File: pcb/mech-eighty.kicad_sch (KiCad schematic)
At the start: 23 parts, among them SW1 Reset, SW2 SW_DPDT_x2, U1 STM32F103C8T6, U2 AMS1117-3.3, Y1 8MHz

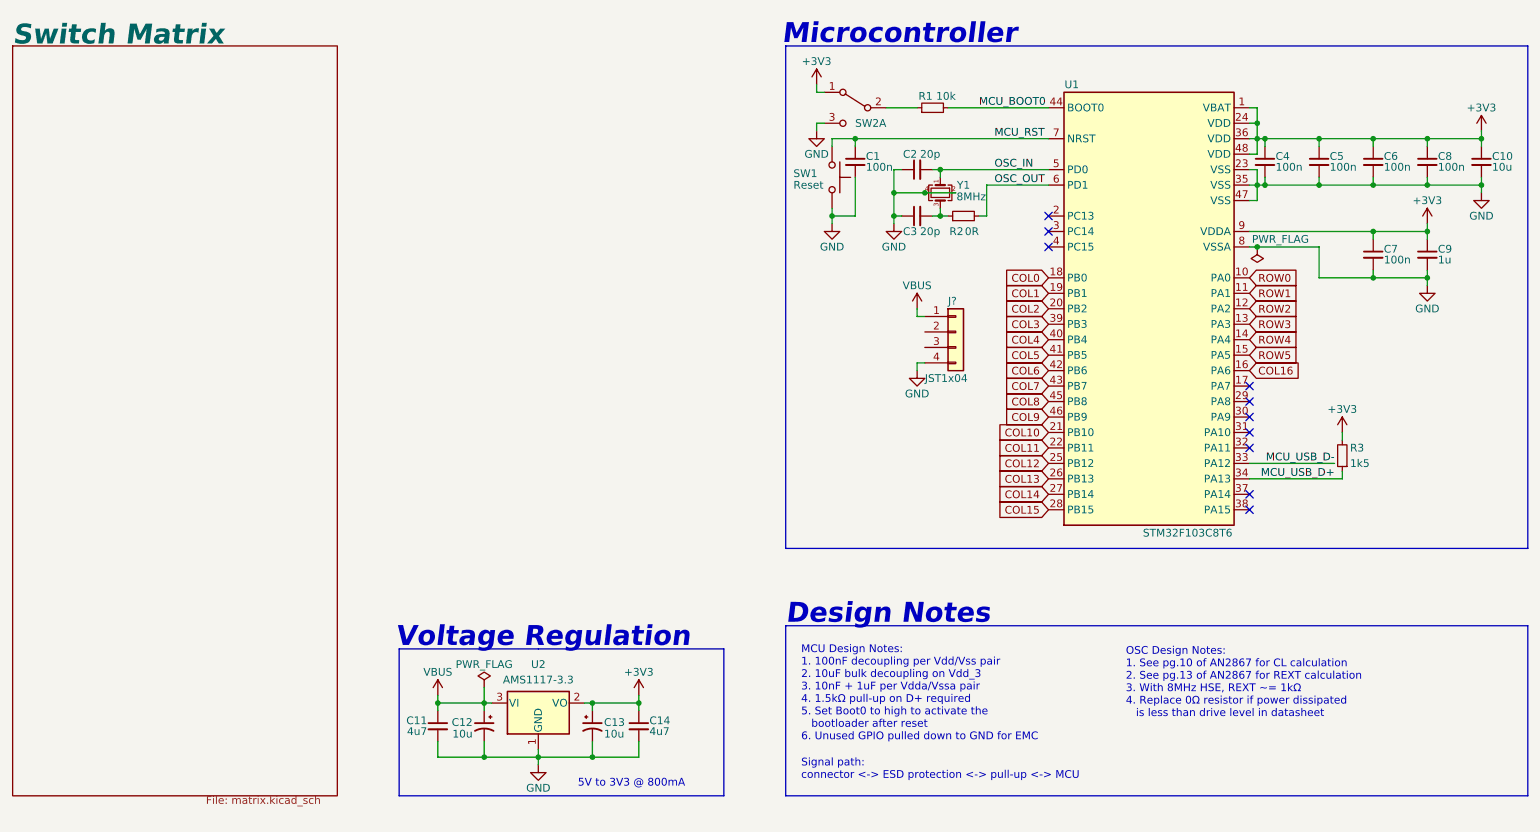
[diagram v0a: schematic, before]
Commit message: Schematic completed
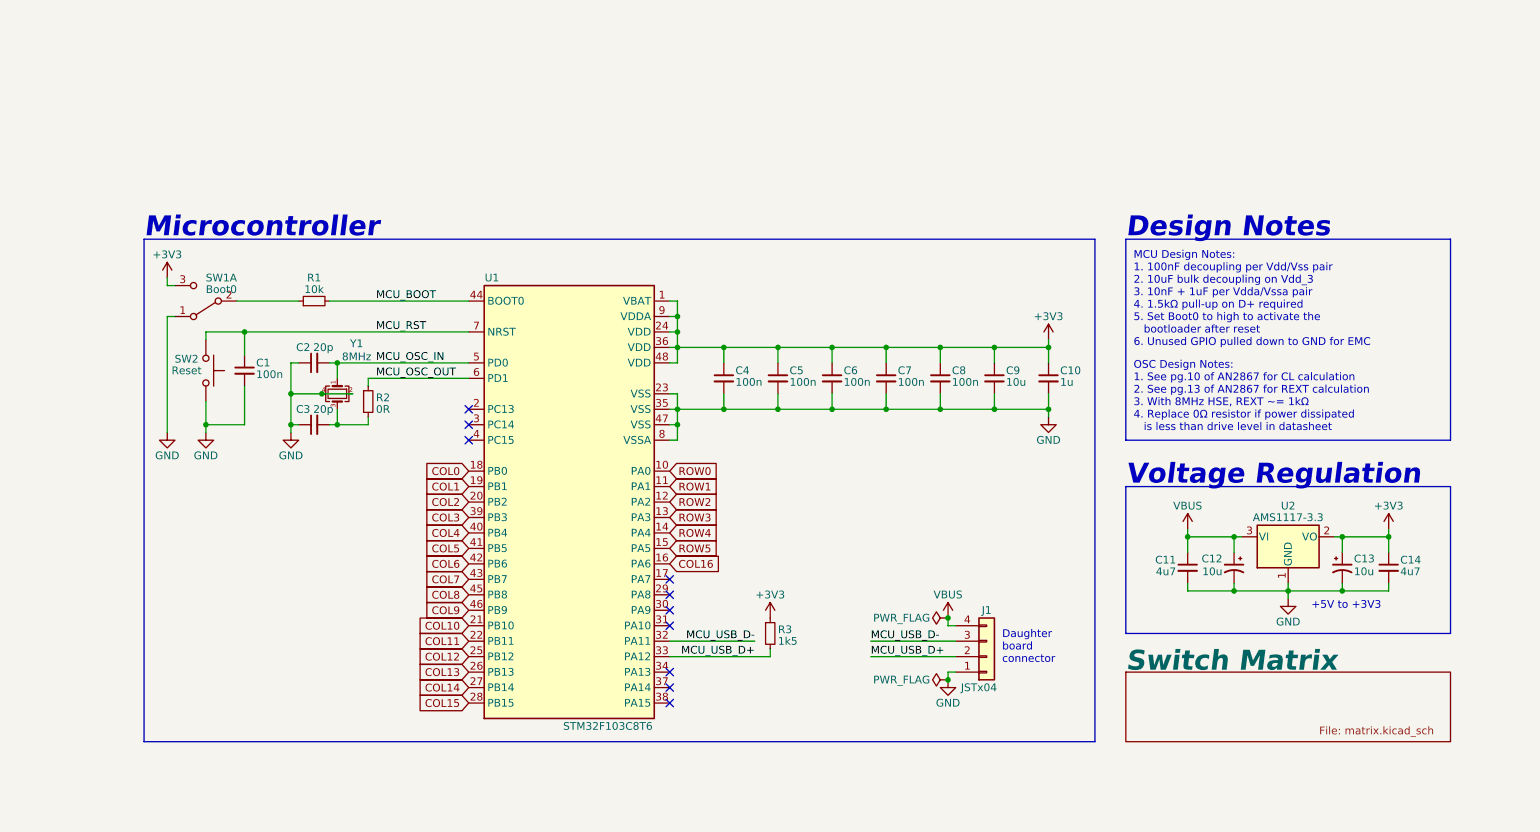
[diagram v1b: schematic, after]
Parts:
- removed J?: JST1x04, symbol Connector_Generic:Conn_01x04
- removed SW1: Reset, footprints:SW_SPST_B3U-1000P, symbol Button_Switch:SW_Push
- removed SW2: SW_DPDT_x2, footprints:SW_SPDT_PCM12, symbol Button_Switch:SW_DPDT_x2
- removed U1: STM32F103C8T6, footprints:LQFP-48-EP_7x7mm_P0.5mm, symbol MCU_ST_STM32F103:STM32F103C8T6
- removed U2: AMS1117-3.3, footprints:SOT-223, symbol Regulator_Linear:AMS1117-3.3
- added J1: JSTx04, connectors:JST-SM04B-GHS-TB_1x4P, symbol Connector-Generic:Conn_01x04
- added SW1: Boot0, switches:SW-SPDT-PCM12, symbol Switches:SW_DPDT_x2
- added SW2: Reset, switches:SW-SPST-B3U-1000P, symbol Switches:SW_Push
- added U1: STM32F103C8T6, packages:LQFP-48, symbol MCU-ST-STM32F103:STM32F103C8T6
- added U2: AMS1117-3.3, packages:SOT-223, symbol Regulator-Linear:AMS1117-3.3
- C1, C2, C3, C4, C5, C6, C7, C8: footprint footprints:C_0603_1608Metric -> capacitors:C-0603-1608
- C10: value 10u -> 1u; footprint footprints:C_0805_2012Metric -> capacitors:C-0805-2012
- C11, C14: footprint footprints:C_0805_2012Metric -> capacitors:C-0805-2012
- C12, C13: footprint footprints:C_3216_18KemetA -> capacitors:C-3216-18A
- C9: value 1u -> 10u; footprint footprints:C_0603_1608Metric -> capacitors:C-0805-2012
- R1, R2, R3: footprint footprints:R_0603_1608Metric -> resistors:R-0603-1608
- Y1: footprint footprints:Crystal-SMD-3225-4P -> crystals:Crystal-SMD-3225-4P
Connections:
- net OSC_OUT is gone; now on an unnamed net: R2.2
- net +3V3: now also R3.1, SW1.3 (C), U1.1 (VBAT), U1.24 (VDD), U1.36 (VDD), U1.48 (VDD), U1.9 (VDDA), U2.2 (VO); no longer R3.2
- net COL0: now also U1.18 (PB0)
- net COL1: now also U1.19 (PB1)
- net COL10: now also U1.21 (PB10)
- net COL11: now also U1.22 (PB11)
- net COL12: now also U1.25 (PB12)
- net COL13: now also U1.26 (PB13)
- net COL14: now also U1.27 (PB14)
- net COL15: now also U1.28 (PB15)
- net COL16: now also U1.16 (PA6)
- net COL2: now also U1.20 (PB2)
- net COL3: now also U1.39 (PB3)
- net COL4: now also U1.40 (PB4)
- net COL5: now also U1.41 (PB5)
- net COL6: now also U1.42 (PB6)
- net COL7: now also U1.43 (PB7)
- net COL8: now also U1.45 (PB8)
- net COL9: now also U1.46 (PB9)
- net GND: now also J1.1 (Pin_1), SW1.1 (A), SW2.2, U1.23 (VSS), U1.35 (VSS), U1.47 (VSS), U1.8 (VSSA), U2.1 (GND)
- net MCU_RST: now also SW2.1, U1.7 (NRST)
- net MCU_USB_D+: now also R3.2, J1.2 (Pin_2), U1.33 (PA12); no longer R3.1
- net MCU_USB_D-: now also J1.3 (Pin_3), U1.32 (PA11)
- net ROW0: now also U1.10 (PA0)
- net ROW1: now also U1.11 (PA1)
- net ROW2: now also U1.12 (PA2)
- net ROW3: now also U1.13 (PA3)
- net ROW4: now also U1.14 (PA4)
- net ROW5: now also U1.15 (PA5)
- net VBUS: now also J1.4 (Pin_4), U2.3 (VI)
- net at R1.1: now also SW1.2 (B)
- net at C3.2, Y1.3: no longer R2.1
- net MCU_BOOT0 renamed MCU_BOOT
- net MCU_BOOT: now also U1.44 (BOOT0)
- net OSC_IN renamed MCU_OSC_IN
- net MCU_OSC_IN: now also U1.5 (PD0)
- new net MCU_OSC_OUT: R2.1, U1.6 (PD1)
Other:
- note added: "+5V to +3V3"
- note added: "Daughter board connector"
- note removed: "5V to 3V3 @ 800mA"
- note removed: "Signal path: connector <-> ESD protection <-> pull-up <-> MCU"

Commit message: Routed matrix and MCU
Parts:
- removed C4: 100n, capacitors:C-0603-1608, symbol Device:C_Small
- renumbered C11 to C10, C12 to C11, C13 to C12, C14 to C13, C5 to C4, C6 to C5, C7 to C6, C8 to C7, C9 to C8, C10 to C9
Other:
- moved on the sheet: C4, C5, C6, C7, C8, C9

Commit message: Routing completed
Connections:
- net COL0: now also U1.19 (PB1); no longer U1.18 (PB0)
- net COL1: now also U1.20 (PB2); no longer U1.19 (PB1)
- net COL10: now also U1.37 (PA14); no longer U1.21 (PB10)
- net COL11: now also U1.38 (PA15); no longer U1.22 (PB11)
- net COL12: now also U1.39 (PB3); no longer U1.25 (PB12)
- net COL13: now also U1.40 (PB4); no longer U1.26 (PB13)
- net COL14: now also U1.41 (PB5); no longer U1.27 (PB14)
- net COL15: now also U1.42 (PB6); no longer U1.28 (PB15)
- net COL16: now also U1.43 (PB7); no longer U1.16 (PA6)
- net COL2: now also U1.21 (PB10); no longer U1.20 (PB2)
- net COL3: now also U1.25 (PB12); no longer U1.39 (PB3)
- net COL4: now also U1.26 (PB13); no longer U1.40 (PB4)
- net COL5: now also U1.27 (PB14); no longer U1.41 (PB5)
- net COL6: now also U1.28 (PB15); no longer U1.42 (PB6)
- net COL7: now also U1.29 (PA8); no longer U1.43 (PB7)
- net COL8: now also U1.30 (PA9); no longer U1.45 (PB8)
- net COL9: now also U1.31 (PA10); no longer U1.46 (PB9)
- net ROW0: now also U1.15 (PA5); no longer U1.10 (PA0)
- net ROW1: now also U1.14 (PA4); no longer U1.11 (PA1)
- net ROW2: now also U1.13 (PA3); no longer U1.12 (PA2)
- net ROW3: now also U1.18 (PB0); no longer U1.13 (PA3)
- net ROW4: now also U1.17 (PA7); no longer U1.14 (PA4)
- net ROW5: now also U1.16 (PA6); no longer U1.15 (PA5)
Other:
- moved on the sheet: R3

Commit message: update
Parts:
- removed C11, C12: 10u, capacitors:C-3216-18A, symbol Device:C_Polarized_Small_US
- removed J1: JSTx04, connectors:JST-SM04B-GHS-TB_1x4P, symbol Connector-Generic:Conn_01x04
- removed SW1: Boot0, switches:SW-SPDT-PCM12, symbol Switches:SW_DPDT_x2
- removed SW2: Reset, switches:SW-SPST-B3U-1000P, symbol Switches:SW_Push
- removed U1: STM32F103C8T6, packages:LQFP-48, symbol MCU-ST-STM32F103:STM32F103C8T6
- removed U2: AMS1117-3.3, packages:SOT-223, symbol Regulator-Linear:AMS1117-3.3
- removed Y1: 8MHz, crystals:Crystal-SMD-3225-4P, symbol Device:Crystal_GND24_Small
- added C11: 1u, Capacitor_SMD:C_0805_2012Metric, symbol Device:C_Small
- added C12: 100n, Capacitor_SMD:C_0603_1608Metric, symbol Device:C_Small
- added C14: 20p, Capacitor_SMD:C_0603_1608Metric, symbol Device:C_Small
- added J1: BM04B-SRSS, Connector_JST:JST_SH_SM04B-SRSS-TB_1x04-1MP_P1.00mm_Horizontal, symbol Connector_Generic:Conn_01x04
- added SW1: MSK-12C02, Button_Switch_SMD:SW_SPDT_PCM12, symbol Button_Switch:SW_DPDT_x2
- added SW2: PTS526-SK15, Button_Switch_SMD:SW_PTS526_SM08_SMTR2_LFS, symbol Button_Switch:SW_Push
- added U1: AMS1117-3.3, Package_TO_SOT_SMD:SOT-223-3_TabPin2, symbol Regulator_Linear:AMS1117-3.3
- added U2: STM32F103C8T6, Package_QFP:LQFP-48_7x7mm_P0.5mm, symbol Custom_Components:STM32F103C8T6
- added Y1: 8MHz, Crystal:Crystal_SMD_HC49-SD, symbol Device:Crystal_Small
- C1, C4: value 100n -> 1u; footprint capacitors:C-0603-1608 -> Capacitor_SMD:C_0805_2012Metric
- C10: value 4u7 -> 100n; footprint capacitors:C-0805-2012 -> Capacitor_SMD:C_0603_1608Metric
- C13: value 4u7 -> 20p; footprint capacitors:C-0805-2012 -> Capacitor_SMD:C_0603_1608Metric
- C2, C3: value 20p -> 10u; footprint capacitors:C-0603-1608 -> Capacitor_SMD:C_0805_2012Metric
- C5, C6, C7: footprint capacitors:C-0603-1608 -> Capacitor_SMD:C_0603_1608Metric
- C8: value 10u -> 100n; footprint capacitors:C-0805-2012 -> Capacitor_SMD:C_0603_1608Metric
- C9: value 1u -> 10u; footprint capacitors:C-0805-2012 -> Capacitor_SMD:C_0805_2012Metric
- R1, R2, R3: footprint resistors:R-0603-1608 -> Resistor_SMD:R_0603_1608Metric
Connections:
- net +3V3: now also C10.1, C3.1, C11.1, SW1.3 (C), U1.2 (VO), U2.1 (VBAT), U2.24 (VDD), U2.36 (VDD), U2.48 (VDD), U2.9 (VDDA); no longer C13.1
- net COL0: now also U2.38 (PA15)
- net COL1: now also U2.28 (PB15)
- net COL10: now also U2.42 (PB6)
- net COL11: now also U2.41 (PB5)
- net COL12: now also U2.40 (PB4)
- net COL13: now also U2.39 (PB3)
- net COL14: now also U2.20 (PB2)
- net COL15: now also U2.19 (PB1)
- net COL16: now also U2.18 (PB0)
- net COL2: now also U2.27 (PB14)
- net COL3: now also U2.26 (PB13)
- net COL4: now also U2.25 (PB12)
- net COL5: now also U2.22 (PB11)
- net COL6: now also U2.21 (PB10)
- net COL7: now also U2.46 (PB9)
- net COL8: now also U2.45 (PB8)
- net COL9: now also U2.43 (PB7)
- net GND: now also C1.1, C3.2, C11.2, C12.2, C14.2, J1.4 (Pin_4), SW1.1 (A), SW2.2, U1.1 (GND), U2.23 (VSS), U2.35 (VSS), U2.47 (VSS), U2.8 (VSSA); no longer C1.2, C3.1
- net MCU_BOOT: now also U2.44 (BOOT0)
- net MCU_OSC_IN: now also C13.1, U2.5 (PD0), Y1.1; no longer C2.2
- net MCU_OSC_OUT: now also R2.2, U2.6 (PD1); no longer R2.1
- net MCU_RST: now also C12.1, SW2.1, U2.7 (NRST); no longer C1.1
- net MCU_USB_D+: now also J1.3 (Pin_3), U2.33 (PA12)
- net MCU_USB_D-: now also J1.2 (Pin_2), U2.32 (PA11)
- net ROW0: now also U2.15 (PA5)
- net ROW1: now also U2.14 (PA4)
- net ROW2: now also U2.13 (PA3)
- net ROW3: now also U2.12 (PA2)
- net ROW4: now also U2.11 (PA1)
- net ROW5: now also U2.10 (PA0)
- net VBUS: now also C1.2, C2.2, J1.1 (Pin_1), U1.3 (VI); no longer C10.1
- net at R1.1: now also SW1.2 (B)
- new net: C14.1, R2.1, Y1.2
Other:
- note added: "*+5V from USBC daughter board"
- note added: "*100nF x Vdd or Vbat or Vdda *1uF decoupling on Vdda"
- note added: "*10uF decoupling on Vdd_3"
- note added: "*FLASH"
- note added: "*RUN"
- note added: "*for CL calculation see AN2867 (pg.10) *for REXT calculation see AN2867 (pg.13) *if power < drive level then replace 0R *REXT ~= 1k @ 8MHz"
- note added: "*regulated +3.3V"
- note added: "Voltage Regulator"
- note added: "boot mode switch"
- note added: "daughter board"
- note added: "reset switch"
- note removed: "+5V to +3V3"
- note removed: "Daughter board connector"
- note removed: "Design Notes"
- note removed: "MCU Design Notes: 1. 100nF decoupling per Vdd/Vss pair 2. 10uF bulk decoupling on Vdd_3 3. 10nF + 1uF per Vdda/Vssa pair 4. 1.5kΩ pull-up on D+ required 5. Set Boot0 to high to activate the bootloader after reset 6. Unused GPIO pulled down to GND for EMC"
- note removed: "OSC Design Notes: 1. See pg.10 of AN2867 for CL calculation 2. See pg.13 of AN2867 for REXT calculation 3. With 8MHz HSE, REXT ~= 1kΩ 4. Replace 0Ω resistor if power dissipated is less than drive level in datasheet"
- note removed: "Voltage Regulation"
- title: mech-eighty -> Mech Eighty
